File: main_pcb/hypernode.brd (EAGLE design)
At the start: 92.5 x 100 mm, 31 parts, among them IC1 74HCT245D, U1 MAX488, X2 JST-XH-CONNECTOR-02-PIN, X4 JST-XH-CONNECTOR-02-PIN, X7 JST-XH-03-PIN-LONG-PAD, X8 JST-XH-03-PIN-LONG-PAD

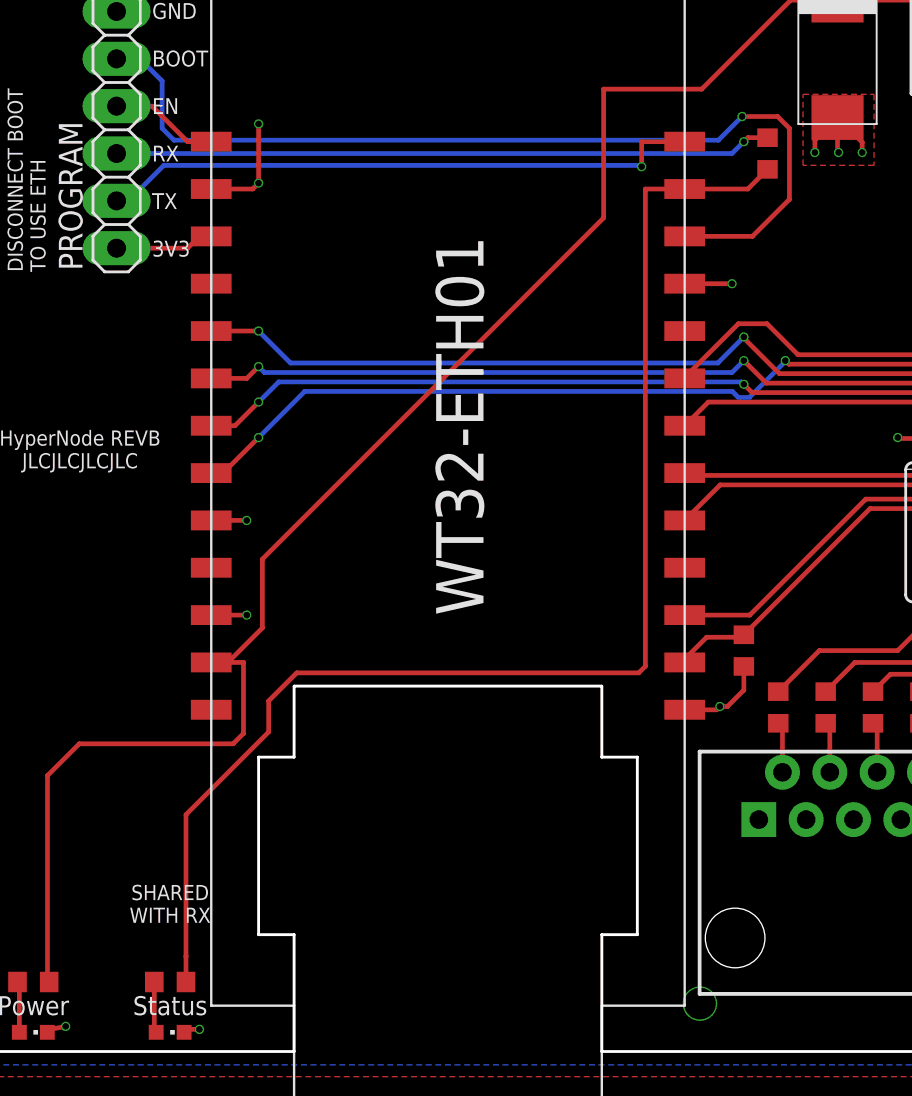
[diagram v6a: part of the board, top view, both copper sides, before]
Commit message: change rx resistor to 2x100r
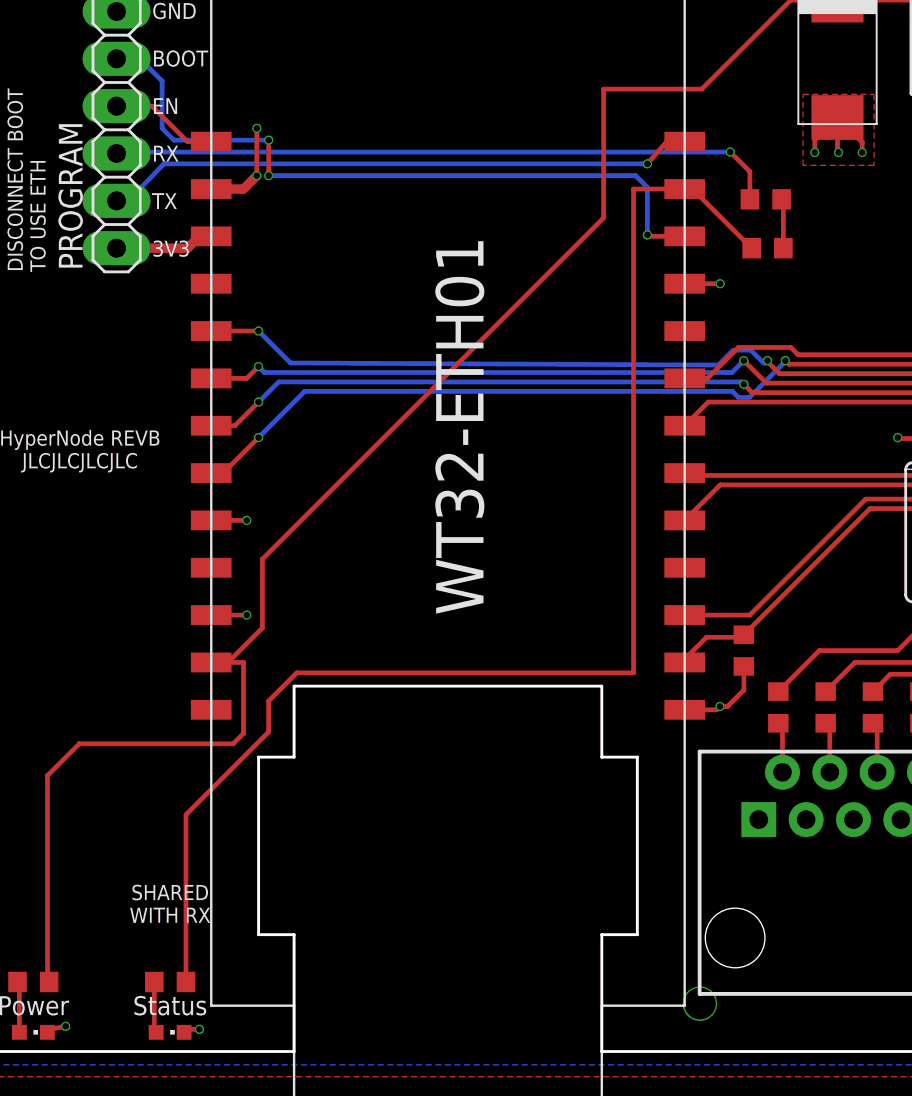
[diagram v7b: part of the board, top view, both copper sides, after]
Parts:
- added R8: 100R, Multischriever:ADAFRUIT_R0603
- R5: value 1K -> 100R
- moved R5 5.08 mm to (47.7, 43.1), turned to 180 degrees
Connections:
- new net N$21: PROGRAM.3, R8.1
- net N$1: now also R8.2; no longer PROGRAM.3
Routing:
- net N$21: track 0.00 -> 35.9 mm, vias 0 -> 1
- net N$1: track 35.3 -> 2.66 mm, vias 1 -> 0
- net IO0: track 50.5 -> 38.6 mm, vias 1 -> 3
- net GND: track 35.8 -> 34.6 mm
- net DMXIN: track 43.9 -> 42.8 mm
- net TX: track 32.7 -> 31.9 mm

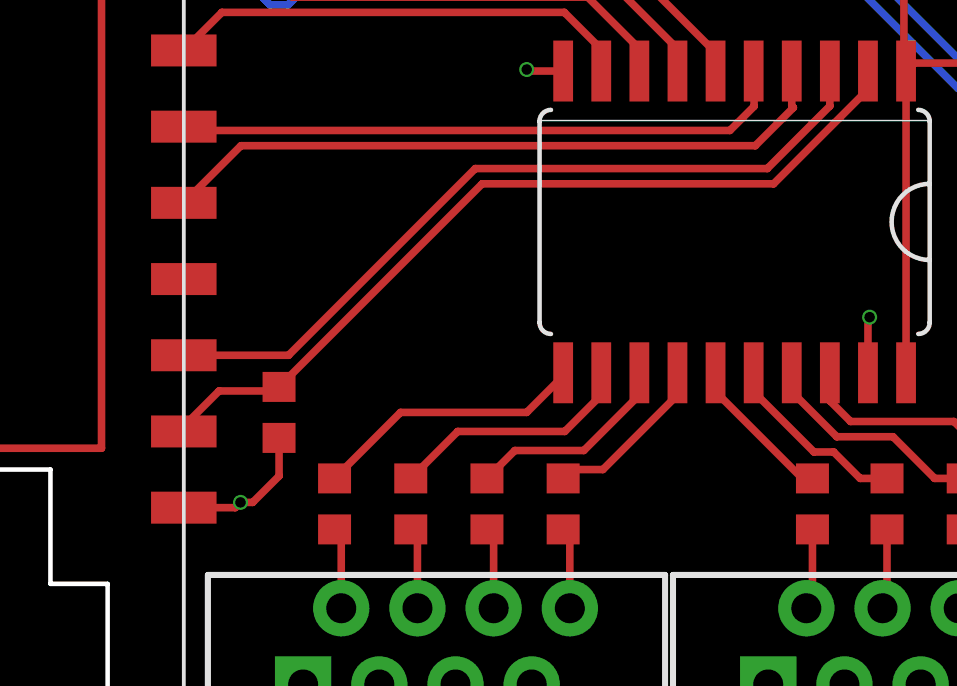
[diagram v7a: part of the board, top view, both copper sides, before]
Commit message: remove unnecessary pull down resistor
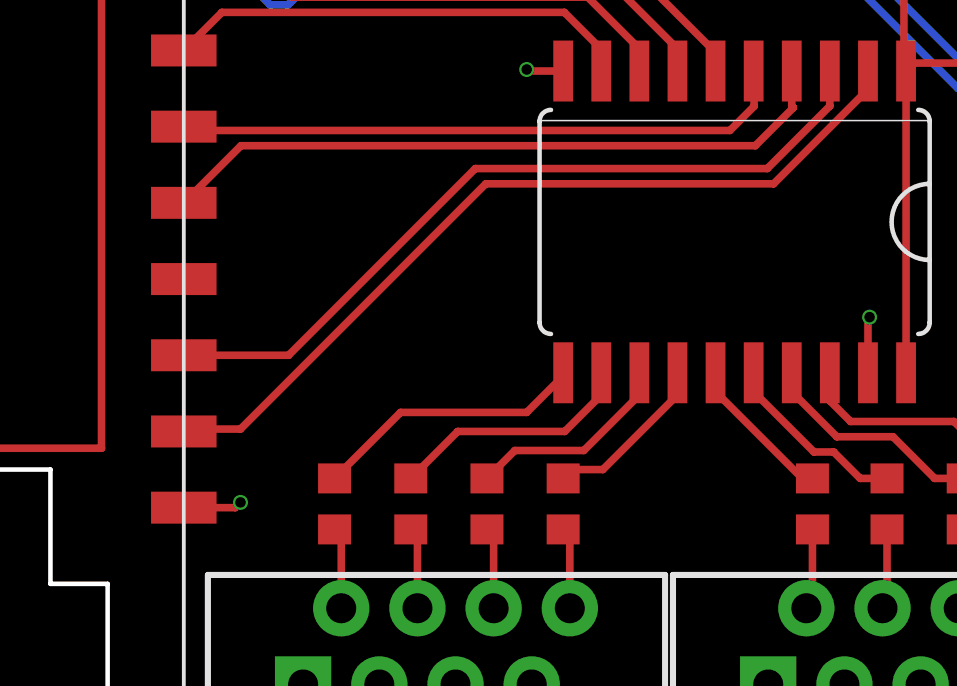
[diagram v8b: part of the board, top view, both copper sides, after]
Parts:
- removed R7: 10K, Multischriever:ADAFRUIT_R0603
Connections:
- net GND: no longer R7.2
- net WS4: no longer R7.1
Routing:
- net GND: track 34.6 -> 31.7 mm
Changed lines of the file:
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@@
 <attribute name="VALUE" x="15.97" y="41.83" size="1.27" layer="27" rot="R90"/>
-</element>
-<element name="R7" library="Multischriever" package="ADAFRUIT_R0603" value="10K" x="46.45" y="21.51" smashed="yes" rot="R270">
-<attribute name="VALUE" x="47.72" y="21.51" size="0.8128" layer="27" font="vector" rot="R270" align="center"/>
 </element>
 <element name="R6" library="Multischriever" package="ADAFRUIT_R0603" value="180R" x="15.67" y="3.73" smashed="yes">
@@
 <contactref element="C2" pad="2"/>
 <contactref element="PROGRAM" pad="6"/>
-<contactref element="R7" pad="2"/>
 <contactref element="LED_STATUS" pad="C"/>
 <polygon width="0.254" layer="16">
@@
 <wire x1="69.89" y1="30.455" x2="69.945" y2="30.4" width="0.254" layer="1"/>
 <via x="69.945" y="30.4" extent="1-16" drill="0.35"/>
-<wire x1="45.165" y1="18.51" x2="45.57" y2="18.51" width="0.254" layer="1"/>
-<wire x1="46.45" y1="20.66" x2="46.45" y2="19.39" width="0.254" layer="1"/>
-<wire x1="46.45" y1="19.39" x2="45.57" y2="18.51" width="0.254" layer="1"/>
 <wire x1="51.475" y1="50.11" x2="50.26" y2="48.895" width="0.254" layer="1"/>
 <wire x1="50.26" y1="48.895" x2="50.26" y2="48.235" width="0.254" layer="1"/>
@@
 <contactref element="U$17" pad="P_IO2"/>
 <contactref element="IC1" pad="2"/>
-<contactref element="R7" pad="1"/>
 <wire x1="66.08" y1="32.8892" x2="66.1562" y2="32.813" width="0.254" layer="1"/>
 <wire x1="66.1562" y1="32.813" x2="66.1562" y2="32.3503875" width="0.254" layer="1"/>
 <wire x1="66.1562" y1="32.3503875" x2="62.9358125" y2="29.13" width="0.254" layer="1"/>
-<wire x1="53.22" y1="29.13" x2="46.45" y2="22.36" width="0.254" layer="1"/>
-<wire x1="62.9358125" y1="29.13" x2="53.22" y2="29.13" width="0.254" layer="1"/>
-<wire x1="46.45" y1="22.36" x2="46.315" y2="22.225" width="0.254" layer="1"/>
-<wire x1="46.315" y1="22.225" x2="44.45" y2="22.225" width="0.254" layer="1"/>
-<wire x1="44.45" y1="22.225" x2="43.275" y2="21.05" width="0.254" layer="1"/>
-<wire x1="43.275" y1="21.05" x2="43.275" y2="20.875" width="0.254" layer="1"/>
+<wire x1="62.9358125" y1="29.13" x2="53.34" y2="29.13" width="0.254" layer="1"/>
+<wire x1="43.275" y1="20.955" x2="43.275" y2="20.875" width="0.254" layer="1"/>
+<wire x1="53.34" y1="29.13" x2="45.165" y2="20.955" width="0.254" layer="1"/>
+<wire x1="45.165" y1="20.955" x2="43.275" y2="20.955" width="0.254" layer="1"/>
 </signal>
 <signal name="WS5">
